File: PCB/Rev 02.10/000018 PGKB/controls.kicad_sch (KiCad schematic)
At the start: 15 parts, among them U3 SN74HCS365PWR

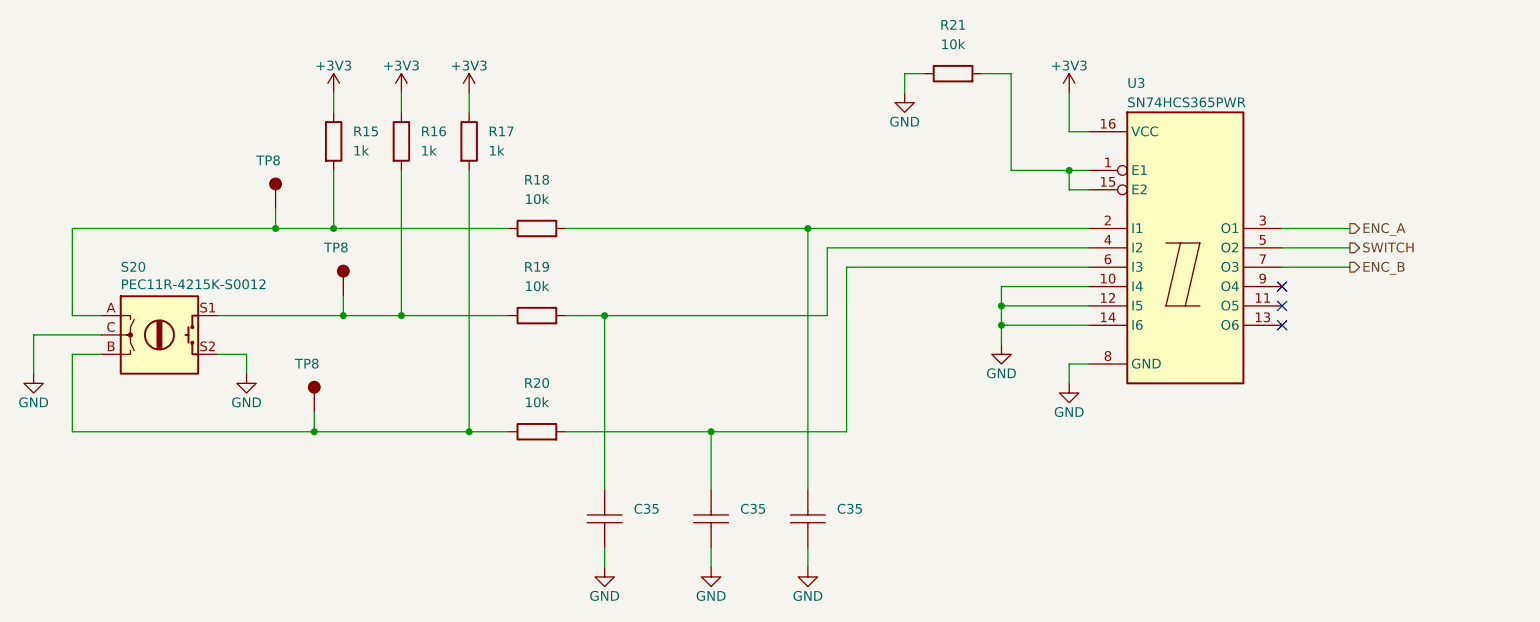
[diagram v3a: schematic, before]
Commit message: Resolved DRC problems
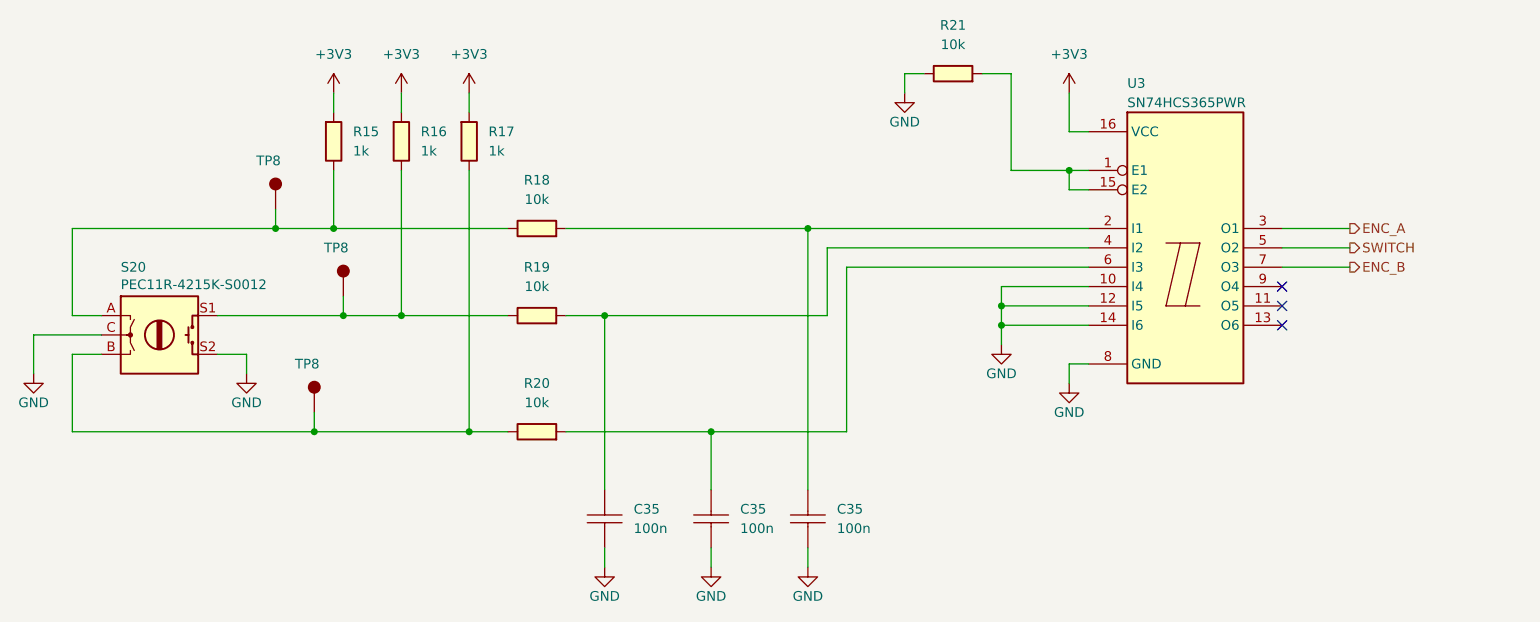
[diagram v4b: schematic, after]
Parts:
- R15, R16, R17: Code 1k -> (none)
- R18, R19, R20, R21: Code 10k -> (none)
- U3: symbol KD_IC_Buffer_Driver_Interface:Schmitt_6CH_SN74HCS365PWR -> KD_IC_Buffer_Driver_Interface:Buffer_Schmitt_6CH_SN74HCS365PWR

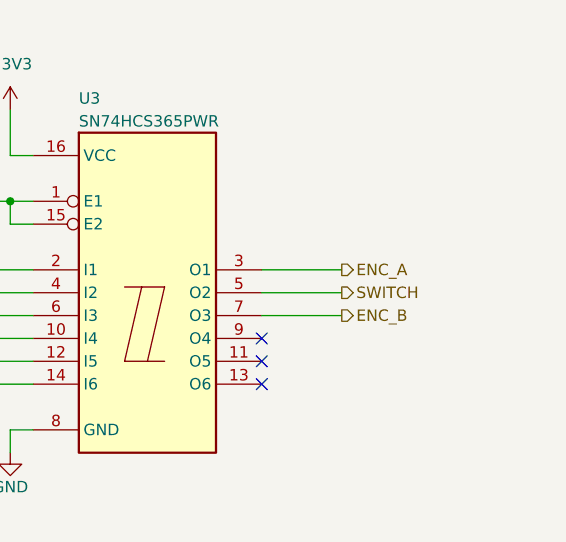
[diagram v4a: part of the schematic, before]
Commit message: Test points for encoder signals
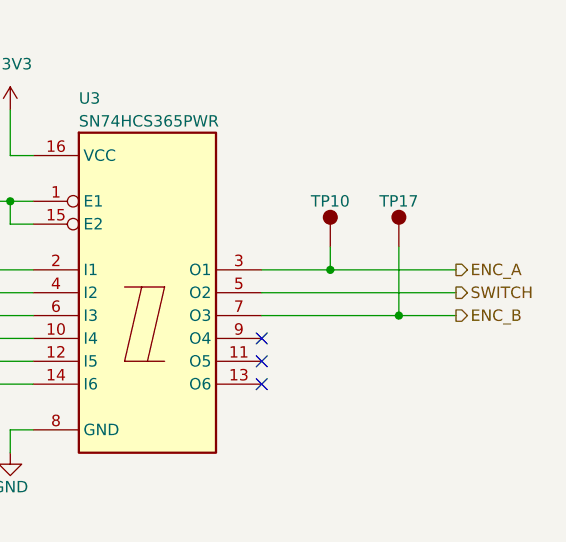
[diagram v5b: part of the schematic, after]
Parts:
- added TP10, TP17: TP D2.5 mm H0.9mm, KD_Connector_Pads:TestPoint_Pad_D2.5mm_H0.9mm, symbol KD_Connector_Pads:TestPoint_2.5mm_H0.9
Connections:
- net ENC_A: now also TP10.1
- net ENC_B: now also TP17.1
